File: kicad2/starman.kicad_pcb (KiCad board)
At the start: 4 copper layers, 195 x 150 mm, 199 parts, among them J1 Conn_01x12, J10 Barrel_Jack_MountingPin, J11 USB_B_Micro, J2 Conn_01x10, J3 Conn_01x12, J4 Conn_01x10, J5 Conn_02x03_Counter_Clockwise, J6 Conn_01x12, J7 Conn_01x10, J8 Conn_01x12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

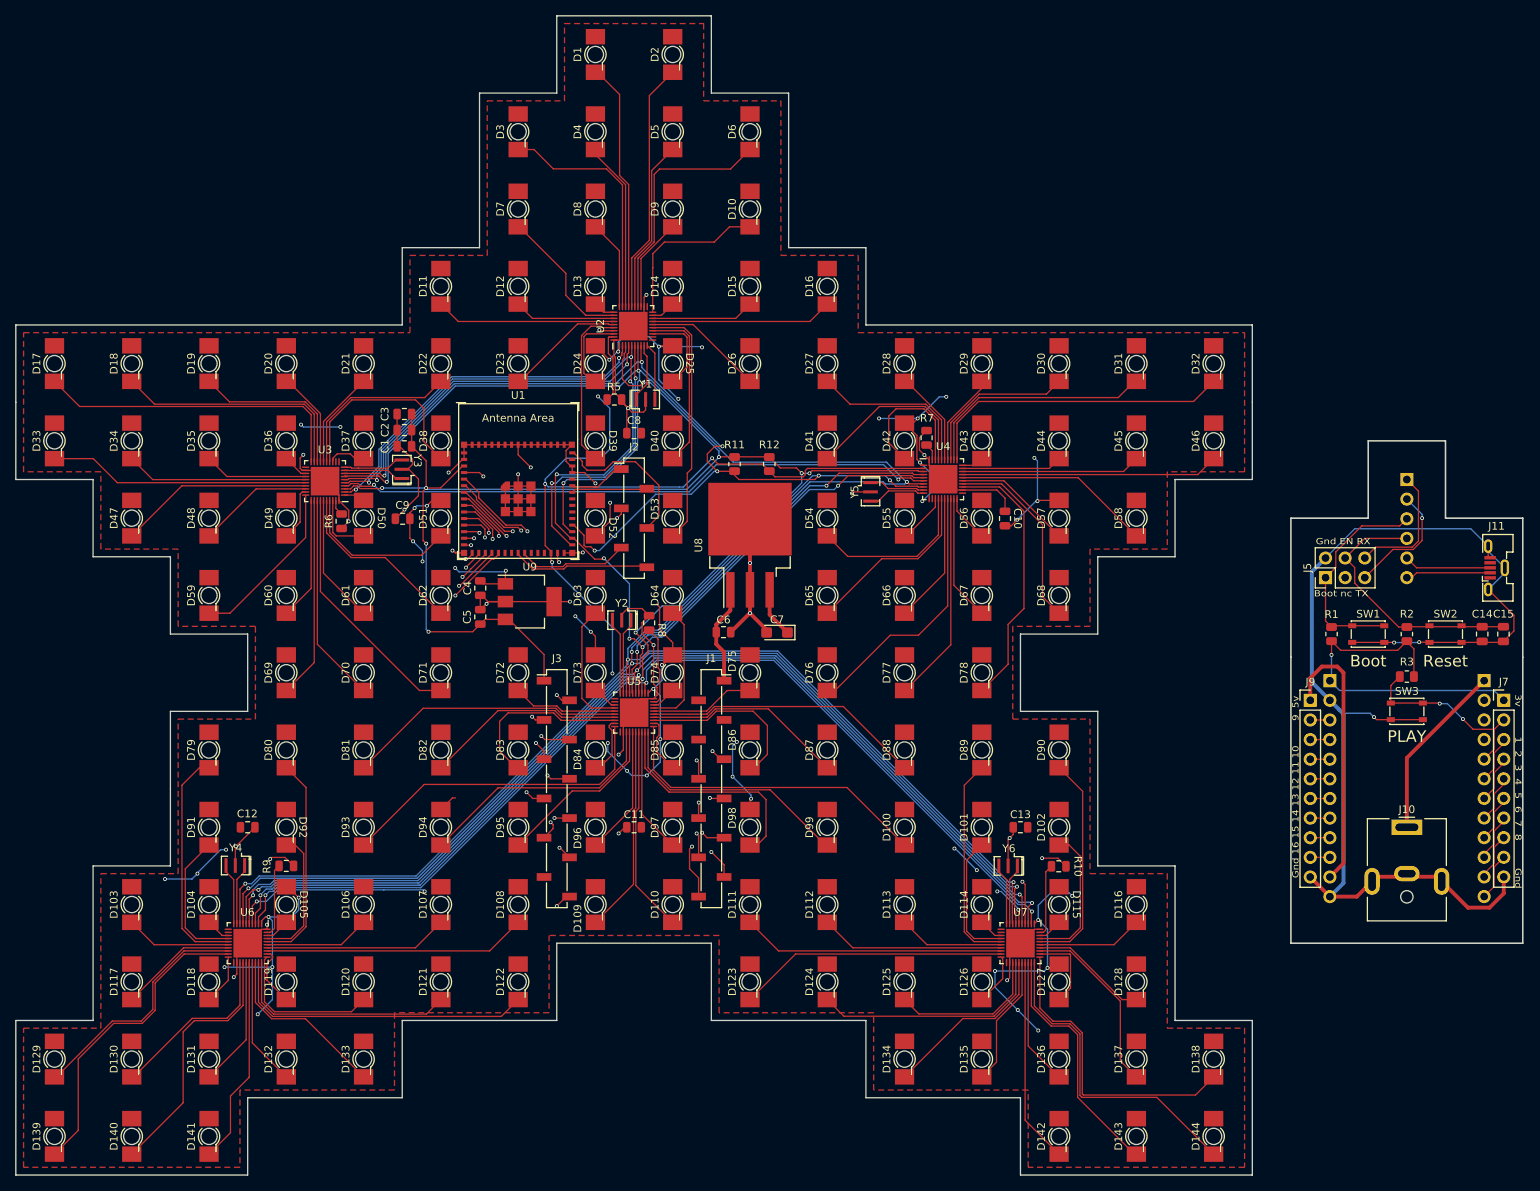
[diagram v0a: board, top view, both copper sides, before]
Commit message: Added sound resistors, channels, volume, and speaker
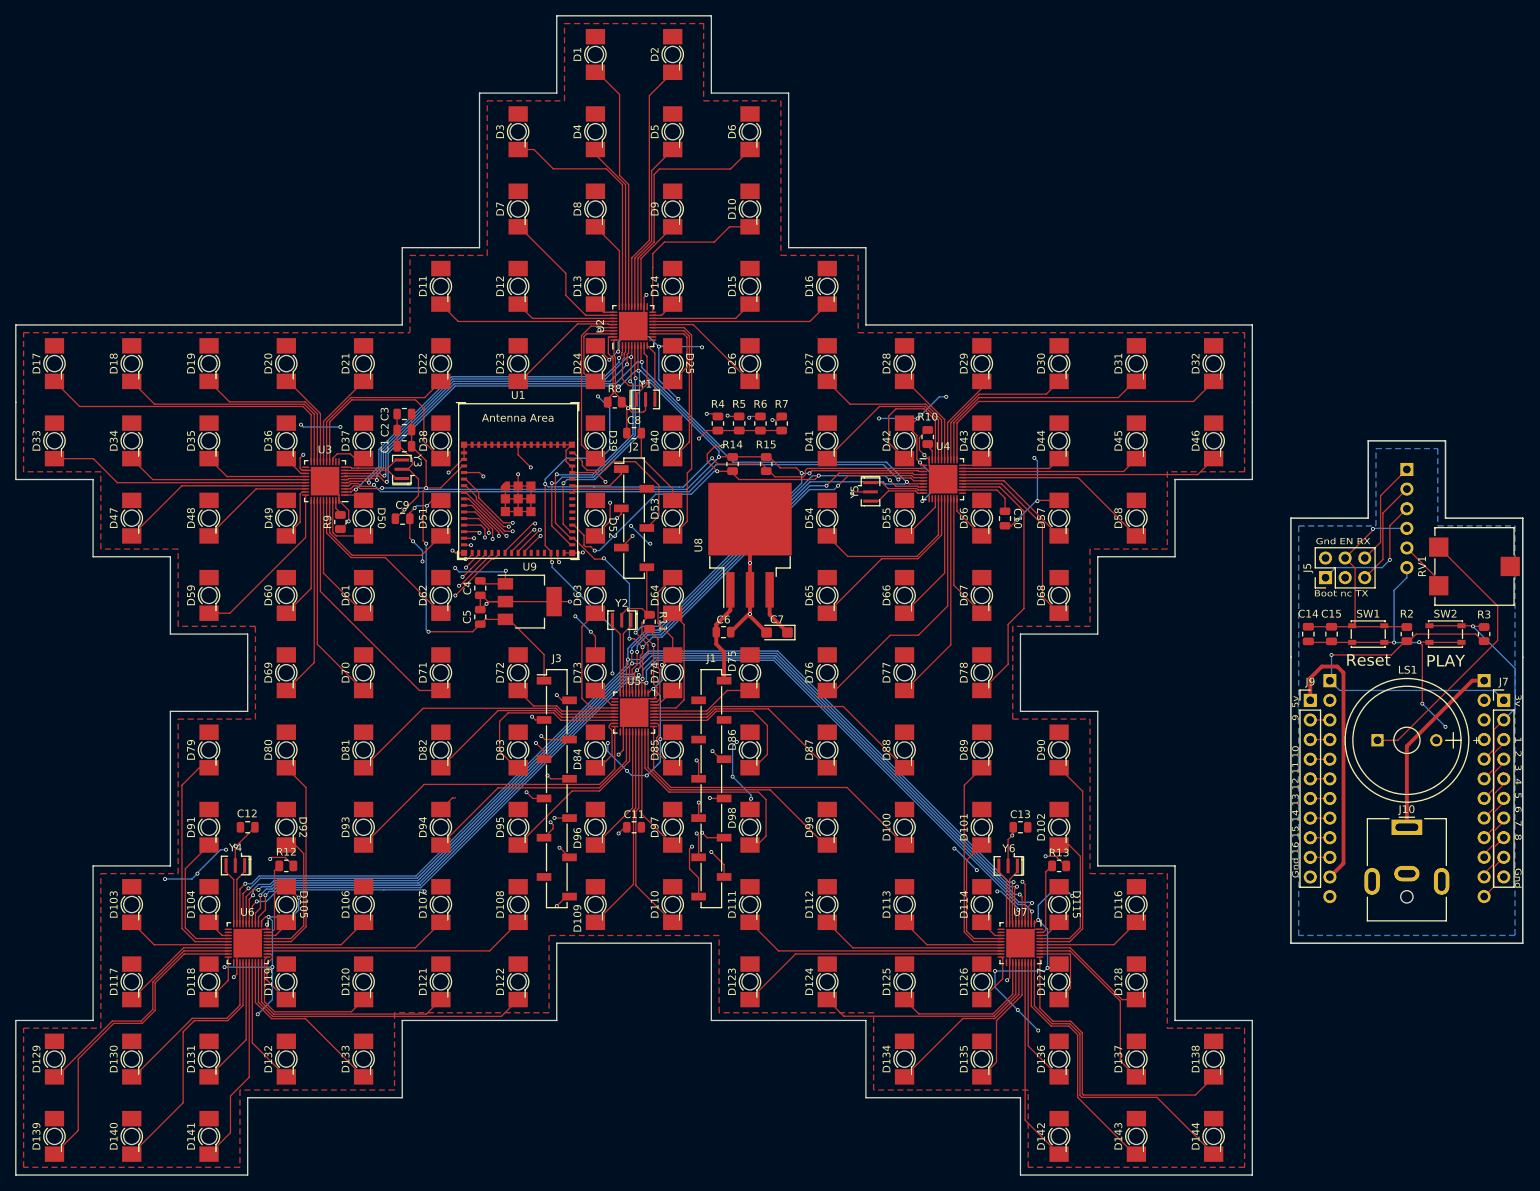
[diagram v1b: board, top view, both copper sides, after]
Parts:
- removed J11: USB_B_Micro, Connector_USB:USB_Micro-B_Molex-105133-0031
- removed R1: 10k, Resistor_SMD:R_0805_2012Metric
- removed SW3: SW_SPST, Button_Switch_SMD:SW_SPST_PTS810
- added LS1: Speaker, Buzzer_Beeper:MagneticBuzzer_StarMicronics_HMB-06_HMB-12, F.Cu at (206.2, 123.8)
- added R13: 3k, Resistor_SMD:R_0805_2012Metric, F.Cu at (165.0, 140.0)
- added R14: 10k, Resistor_SMD:R_0805_2012Metric, F.Cu at (122.8, 88.0)
- added R15: 10k, Resistor_SMD:R_0805_2012Metric, F.Cu at (127.1, 88.0)
- added R4: 75, Resistor_SMD:R_0805_2012Metric, F.Cu at (120.8, 82.8)
- added RV1: 10k, Potentiometer_SMD:Potentiometer_ACP_CA9-VSMD_Vertical, F.Cu at (218.8, 101.2)
- J4: value Conn_01x10 -> Conn_01x06
- R11, R12: value 10k -> 3k
- R5, R6, R7: value 3k -> 75
- moved R12 81.3 mm to (65.0, 140.0), turned to 180 degrees
- moved R10 58.1 mm to (148.0, 84.5), turned to -90 degrees
- moved R6 55.7 mm to (126.3, 82.8)
- moved R9 45.0 mm to (72.0, 95.5), turned to 90 degrees
- moved R8 28.9 mm to (107.5, 80.0), turned to 180 degrees
- moved R11 23.2 mm to (112.0, 108.4)
- moved C14 22.5 mm to (197.2, 110.0)
- moved C15 22.2 mm to (200.2, 110.0)
- moved R7 18.8 mm to (129.1, 82.8), turned to 90 degrees
- moved R5 16.4 mm to (123.6, 82.8), turned to 90 degrees
- moved R3 11.4 mm to (220.0, 110.0), turned to -90 degrees
- moved J4 1.30 mm to (210.0, 88.7)
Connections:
- J2 pad 5: /USBDP -> /SOUND
- J2 pad 6: /USBDM -> GND
- J4 pad 5: /ext_USBDP -> /ext_SOUND
- J4 pad 6: /ext_USBDM -> GNDA
- R11 pad 1: +3V3 -> GND
- R11 pad 2: /OE -> Net-(R11-Pad2)
- R12 pad 1: +3V3 -> GND
- R12 pad 2: /RESET -> Net-(R12-Pad2)
- R5 pad 1: GND -> /SOUND
- R6 pad 1: GND -> /SOUND
- R7 pad 1: GND -> /SOUND
- SW1 pad 1: /ext_GPIO0 -> /ext_EN
- SW2 pad 1: /ext_EN -> /ext_GPIO1
- U1 pad 21: unconnected-(U1-Pad21) -> Net-(R4-Pad2)
- U1 pad 22: unconnected-(U1-Pad22) -> Net-(R5-Pad2)
- U1 pad 23: /USBDM -> Net-(R6-Pad2)
- U1 pad 24: /USBDP -> Net-(R7-Pad2)
- U2 pad 39: Net-(R5-Pad2) -> Net-(R8-Pad2)
- U3 pad 39: Net-(R6-Pad2) -> Net-(R9-Pad2)
- U4 pad 39: Net-(R7-Pad2) -> Net-(R10-Pad2)
- U5 pad 39: Net-(R8-Pad2) -> Net-(R11-Pad2)
- U6 pad 39: Net-(R9-Pad2) -> Net-(R12-Pad2)
- U7 pad 39: Net-(R10-Pad2) -> Net-(R13-Pad2)
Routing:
- net GNDA: track 151.3 -> 42.7 mm, vias 3 -> 4
- net Net-(R7-Pad2): track 2.22 -> 40.7 mm, vias 0 -> 2
- net Net-(R6-Pad2): track 2.04 -> 38.8 mm, vias 0 -> 2
- net Net-(LS1-Pad1): track 0.00 -> 36.1 mm
- net Net-(R4-Pad2): track 0.00 -> 35.3 mm, vias 0 -> 2
- net /SOUND: track 0.00 -> 29.4 mm, vias 0 -> 2
- net Net-(R5-Pad2): track 9.33 -> 37.0 mm, vias 0 -> 2
- net +5V: track 232.8 -> 250.7 mm, vias 48 -> 50
- net /USBDM: track 17.8 -> 0.00 mm
- net /USBDP: track 14.4 -> 0.00 mm
- net /ext_GPIO0: track 28.5 -> 16.8 mm, vias 0 -> 1
- net /ext_USBDP: track 11.3 -> 0.00 mm
- net /ext_USBDM: track 11.0 -> 0.00 mm
- net Net-(R11-Pad2): track 0.00 -> 10.4 mm
- net Net-(R12-Pad2): track 0.00 -> 9.59 mm
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- added copper zone on B.Cu, net GNDA
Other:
- board text removed: "Boot"

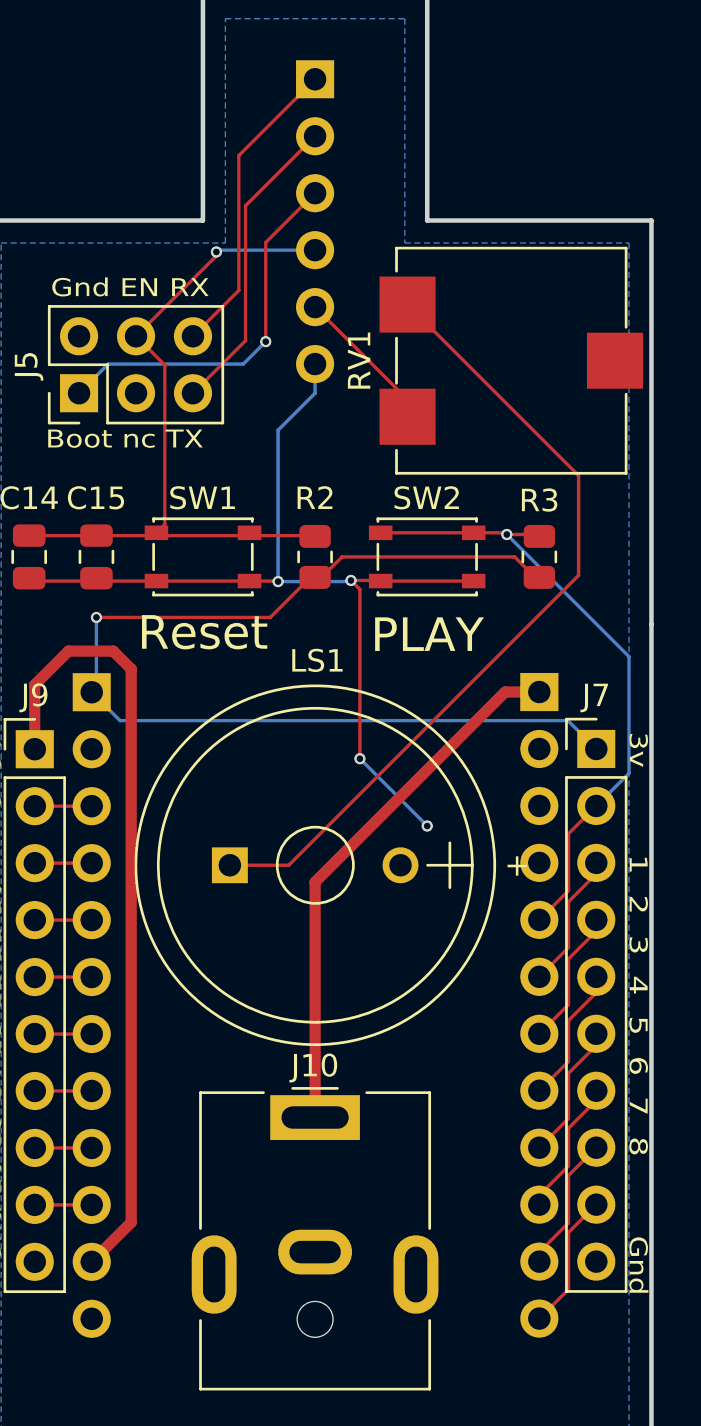
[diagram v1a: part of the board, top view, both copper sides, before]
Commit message: Fixed DRC errors
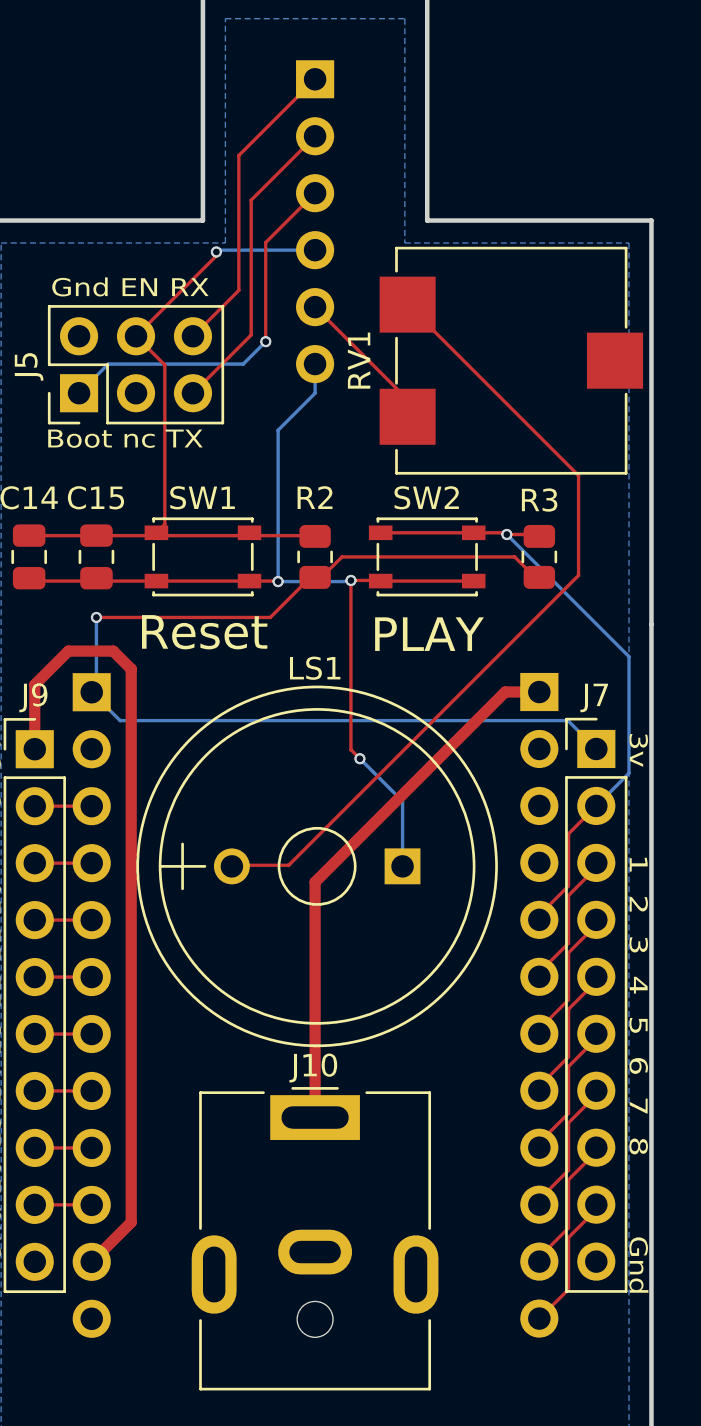
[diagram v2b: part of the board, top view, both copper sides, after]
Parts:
- moved LS1 7.70 mm to (213.9, 123.8), turned to 180 degrees
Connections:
- LS1 pad 1: Net-(LS1-Pad1) -> GNDA
- LS1 pad 2: GNDA -> Net-(RV1-Pad3)
- RV1 pad 3: Net-(LS1-Pad1) -> Net-(RV1-Pad3)
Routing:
- net Net-(RV1-Pad3): track 0.00 -> 36.1 mm
- net Net-(LS1-Pad1): track 36.1 -> 0.00 mm
- net GNDA: track 42.7 -> 44.0 mm, vias 4 -> 3
